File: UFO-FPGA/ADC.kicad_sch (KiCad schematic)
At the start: 7 parts, among them U10 TL071, U12 MAX11116AUT+T

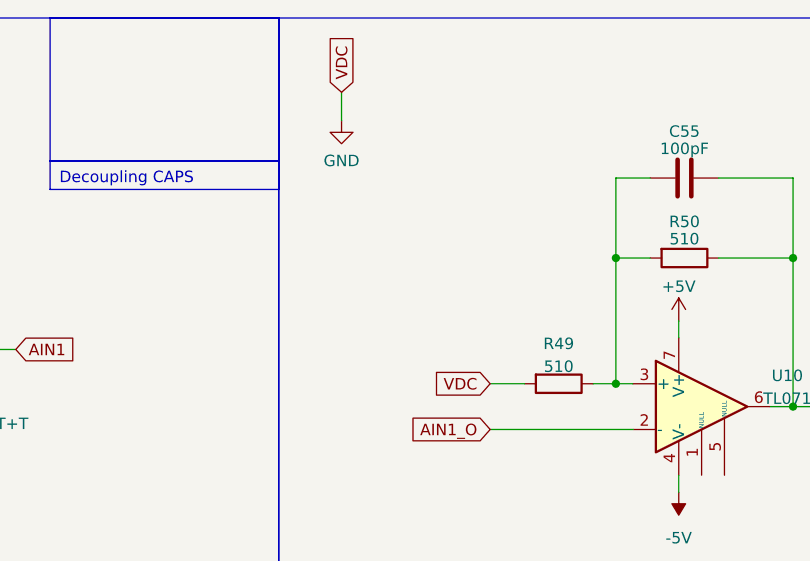
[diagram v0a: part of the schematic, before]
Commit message: PCB planes
Added:
added Power plane +1v2, +3v3 and +5v on layer 4
Ground plane on layer 2 and 5
Added signal layer 1,3 and 6
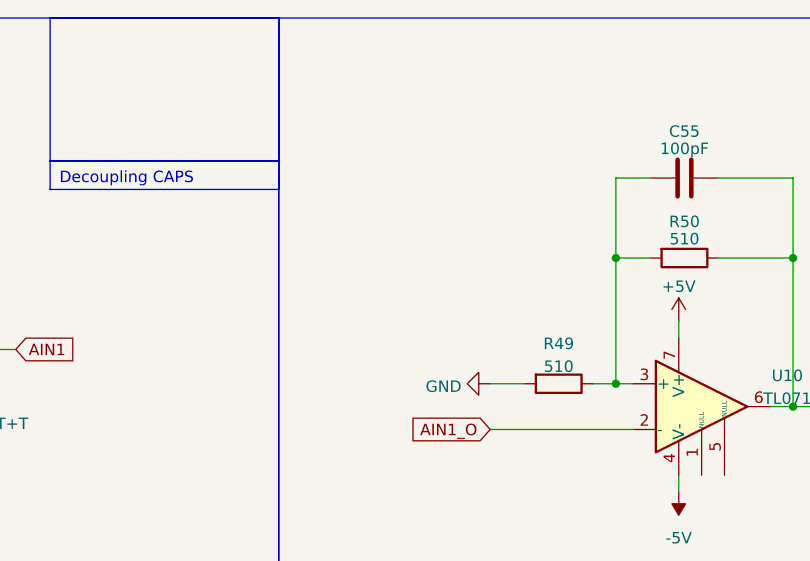
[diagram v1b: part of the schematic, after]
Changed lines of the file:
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@@
-    (stroke (width 0) (type default))
-  )
-  (wire (pts (xy 111.125 26.67) (xy 111.125 29.845))
     (stroke (width 0) (type default))
   )
@@
     )
   )
-  (global_label "VDC" (shape input) (at 127.635 59.055 180) (fields_autoplaced)
-    (effects (font (size 1.27 1.27)) (justify right))
-    (property "Intersheetrefs" "${INTERSHEET_REFS}" (at 121.1006 59.055 0)
-      (effects (font (size 1.27 1.27)) (justify right) hide)
-    )
-  )
   (global_label "AIN1_O" (shape input) (at 127.635 64.135 180) (fields_autoplaced)
     (effects (font (size 1.27 1.27)) (justify right))
@@
     )
   )
-  (global_label "VDC" (shape input) (at 111.125 26.67 90) (fields_autoplaced)
-    (effects (font (size 1.27 1.27)) (justify left))
-    (property "Intersheetrefs" "${INTERSHEET_REFS}" (at 111.125 20.1356 90)
-      (effects (font (size 1.27 1.27)) (justify left) hide)
-    )
-  )
   (global_label "AIN1" (shape input) (at 74.93 55.245 0) (fields_autoplaced)
     (effects (font (size 1.27 1.27)) (justify left))
@@
     )
   )
-  (symbol (lib_id "power:GND") (at 111.125 29.845 0) (unit 1)
-    (in_bom yes) (on_board yes) (dnp no) (fields_autoplaced)
-    (property "Reference" "#PWR049" (at 111.125 36.195 0)
-      (effects (font (size 1.27 1.27)) hide)
-    )
-    (property "Value" "GND" (at 111.125 34.29 0)
-      (effects (font (size 1.27 1.27)))
-    )
-    (property "Footprint" "" (at 111.125 29.845 0)
-      (effects (font (size 1.27 1.27)) hide)
-    )
-    (property "Datasheet" "" (at 111.125 29.845 0)
-      (effects (font (size 1.27 1.27)) hide)
-    )
+  (symbol (lib_id "power:GND") (at 127.635 59.055 270) (unit 1)
+    (in_bom yes) (on_board yes) (dnp no) (fields_autoplaced)
+    (property "Reference" "#PWR049" (at 121.285 59.055 0)
+      (effects (font (size 1.27 1.27)) hide)
+    )
+    (property "Value" "GND" (at 124.4601 59.3718 90)
+      (effects (font (size 1.27 1.27)) (justify right))
+    )
+    (property "Footprint" "" (at 127.635 59.055 0)
+      (effects (font (size 1.27 1.27)) hide)
+    )
+    (property "Datasheet" "" (at 127.635 59.055 0)
+      (effects (font (size 1.27 1.27)) hide)
+    )

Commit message: PCB
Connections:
- net +5V: now also U10.3 (V+); no longer U10.7 (V+)
- net -5V: now also U10.2 (V-); no longer U10.4 (V-)
- net AIN1_O: now also U10.4 (-); no longer U10.2 (-)
- net In-tl71: now reaches C55.1, R49.1, R50.2
- net In-tl71: now also U10.5 (+); no longer U10.3 (+)
- net Out-tl71: now reaches C55.2, R50.1, R51.2
- net Out-tl71: now also U10.1; no longer U10.6
- no-connect marks 0 -> 2
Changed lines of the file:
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@@
   (junction (at 178.435 61.595) (diameter 0) (color 0 0 0 0)
   )
+  (no_connect (at 153.67 69.215))
+  (no_connect (at 151.13 69.215))
   (wire (pts (xy 141.605 59.055) (xy 143.51 59.055))
     (stroke (width 0) (type default))
@@
     (fill (type none))
     (effects (font (size 1.27 1.27)) (justify left top))
+  )
+  (label "Out-tl71" (at 161.29 53.34 0) (fields_autoplaced)
+    (effects (font (size 1.27 1.27)) (justify left bottom))
+  )
+  (label "In-tl71" (at 141.605 51.435 180) (fields_autoplaced)
+    (effects (font (size 1.27 1.27)) (justify right bottom))
   )
   (global_label "AIN1" (shape input) (at 185.42 61.595 0) (fields_autoplaced)
@@
       (effects (font (size 1.27 1.27)))
     )
-    (property "Footprint" "Package_TO_SOT_SMD:SOT-23-5_HandSoldering" (at 152.4 60.325 0)
-      (effects (font (size 1.27 1.27)) hide)
-    )
-    (property "Datasheet" "http://www.ti.com/lit/ds/symlink/tl071.pdf" (at 154.94 57.785 0)
+    (property "Footprint" "Package_TO_SOT_SMD:SOT-23-5_HandSoldering" (at 153.035 82.55 0)
+      (effects (font (size 1.27 1.27)) hide)
+    )
+    (property "Datasheet" "http://www.ti.com/lit/ds/symlink/tl071.pdf" (at 154.94 80.01 0)
       (effects (font (size 1.27 1.27)) hide)
     )
@@
     (pin "4")
     (pin "5")
-    (pin "6")
-    (pin "7")
-    (pin "8")
-    (instances
-      (project "UFO-FPGA"
+    (instances
+      (project "UFO-FPGA"

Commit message: pcb prog redesign
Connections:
- net -5V is gone; now on net GND: U10.2 (V-)
- no-connect marks 2 -> 0
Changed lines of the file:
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@@
   (junction (at 178.435 61.595) (diameter 0) (color 0 0 0 0)
   )
-  (no_connect (at 153.67 69.215))
-  (no_connect (at 151.13 69.215))
   (wire (pts (xy 141.605 59.055) (xy 143.51 59.055))
     (stroke (width 0) (type default))
@@
     )
   )
+  (symbol (lib_id "power:GND") (at 148.59 71.12 0) (unit 1)
+    (in_bom yes) (on_board yes) (dnp no) (fields_autoplaced)
+    (property "Reference" "#PWR036" (at 148.59 77.47 0)
+      (effects (font (size 1.27 1.27)) hide)
+    )
+    (property "Value" "GND" (at 148.59 75.2555 0)
+      (effects (font (size 1.27 1.27)))
+    )
+    (property "Footprint" "" (at 148.59 71.12 0)
+      (effects (font (size 1.27 1.27)) hide)
+    )
+    (property "Datasheet" "" (at 148.59 71.12 0)
+      (effects (font (size 1.27 1.27)) hide)
+    )
+    (pin "1")
+    (instances
+      (project "UFO-FPGA"
+        (path "/b3168f6a-c732-41d3-aeeb-d97dd2f1bb65/98332e8f-475b-462b-a153-03883f4d2670"
+          (reference "#PWR036") (unit 1)
+        )
+      )
+    )
+  )
   (symbol (lib_id "Device:R") (at 149.225 45.085 270) (unit 1)
     (in_bom yes) (on_board yes) (dnp no) (fields_autoplaced)
@@
         )
       )
-    )
-  )
-  (symbol (lib_id "power:-5V") (at 148.59 71.12 180) (unit 1)
-    (in_bom yes) (on_board yes) (dnp no) (fields_autoplaced)
-    (property "Reference" "#PWR062" (at 148.59 73.66 0)
-      (effects (font (size 1.27 1.27)) hide)
-    )
-    (property "Value" "-5V" (at 148.59 76.2 0)
-      (effects (font (size 1.27 1.27)))
-    )
-    (property "Footprint" "" (at 148.59 71.12 0)
-      (effects (font (size 1.27 1.27)) hide)
-    )
-    (property "Datasheet" "" (at 148.59 71.12 0)
-      (effects (font (size 1.27 1.27)) hide)
-    )
-    (pin "1")
-    (instances
-      (project "UFO-FPGA"
-        (path "/b3168f6a-c732-41d3-aeeb-d97dd2f1bb65/abe08156-b909-4d2d-ad35-f723f4a728d5"
-          (reference "#PWR062") (unit 1)
-        )
-        (path "/b3168f6a-c732-41d3-aeeb-d97dd2f1bb65/98332e8f-475b-462b-a153-03883f4d2670"
-          (reference "#PWR065") (unit 1)
-        )
-      )

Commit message: pcb 0603
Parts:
- C55, C56: footprint Capacitor_SMD:C_0805_2012Metric_Pad1.18x1.45mm_HandSolder -> Capacitor_SMD:C_0603_1608Metric_Pad1.08x0.95mm_HandSolder
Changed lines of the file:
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@@
       (effects (font (size 1.27 1.27)))
     )
-    (property "Footprint" "Capacitor_SMD:C_0805_2012Metric_Pad1.18x1.45mm_HandSolder" (at 153.035 35.2298 0)
+    (property "Footprint" "Capacitor_SMD:C_0603_1608Metric_Pad1.08x0.95mm_HandSolder" (at 153.035 35.2298 0)
       (effects (font (size 1.27 1.27)) hide)
     )
@@
       (effects (font (size 1.27 1.27)) (justify right))
     )
-    (property "Footprint" "Capacitor_SMD:C_0805_2012Metric_Pad1.18x1.45mm_HandSolder" (at 177.4698 61.595 0)
-      (effects (font (size 1.27 1.27)) hide)
-    )
+    (property "Footprint" "Capacitor_SMD:C_0603_1608Metric_Pad1.08x0.95mm_HandSolder" (at 177.4698 61.595 0)
+      (effects (font (size 1.27 1.27)) hide)
+    )

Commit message: pcb
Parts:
- removed C55, C56: 100pF, Capacitor_SMD:C_0603_1608Metric_Pad1.08x0.95mm_HandSolder, symbol Device:C
- removed R49, R50: 510, Resistor_SMD:R_0805_2012Metric, symbol Device:R
- removed R51: 10, Resistor_SMD:R_0805_2012Metric, symbol Device:R
- removed U10: TL071, Package_TO_SOT_SMD:SOT-23-5_HandSoldering, symbol Amplifier_Operational:TL071

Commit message: PCB
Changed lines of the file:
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@@
     (stroke (width 0) (type default))
-  )
-  (rectangle (start 78.74 18.415) (end 104.14 34.29)
-    (stroke (width 0) (type default))
-    (fill (type none))
   )
   (rectangle (start 19.05 18.415) (end 104.14 94.615)
@@
     (fill (type none))
   )
-  (rectangle (start 104.14 18.415) (end 277.495 94.615)
-    (stroke (width 0) (type default))
-    (fill (type none))
-  )
-  (text_box "Dit is opamp input voor de ADC. Enige probleem is dat wij niet weten waar de VDC aangeconnect moet worden hierom een label.\n"
-    (at 104.14 85.09 0) (size 173.355 9.525)
-    (stroke (width 0) (type default))
-    (fill (type none))
-    (effects (font (size 1.27 1.27)) (justify left top))
-  )
-  (text_box "Decoupling CAPS"
-    (at 78.74 34.29 0) (size 25.4 3.175)
-    (stroke (width 0) (type default))
-    (fill (type none))
-    (effects (font (size 1.27 1.27)) (justify left top))
-  )
-  (text_box "Dit is de ADC. De ADC kan twee singalen meten via AIN1 en AIN2. De singalen moeten geleverd worden door een een opamp DIe de gebruiker zelf moet leveren. Dit geeft de gebruiker ook weer meer flexibiliteit en overegens een kleiner PCB."
+  (text_box "Dit is de ADC. De ADC kan twee singalen meten via AIN1. De singalen moeten geleverd worden door een een opamp Die de gebruiker zelf moet leveren. Dit geeft de gebruiker ook weer meer flexibiliteit en overegens een kleiner PCB."
     (at 19.05 85.09 0) (size 85.09 9.525)
     (stroke (width 0) (type default))
